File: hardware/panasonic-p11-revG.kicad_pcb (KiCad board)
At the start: 2 copper layers, 48.5 x 18 mm, 10 parts, among them J1 1x4, J11 1.27_RA_8way, J2 1x4

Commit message: hardware: J1/J2 expansion headers to 2.54mm pitch
Standard 0.1in header spacing with 1.7mm pads, repositioned to clear the
tie holes and board edge; re-routed and re-verified (all 14 nets correct,
CNT pin 4 isolated, 0 DRC, silk clean). Gerber zip regenerated.

Co-Authored-By: Claude Opus 5 <noreply@anthropic.com>
Claude-Session: https://claude.ai/code/session_01BQkgfhAH12YMdeYMtUUmA3
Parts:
- J1: footprint local:J2 -> local:J1
- J2: footprint local:J3 -> local:J2
- moved J1 1.63 mm to (60.0, 24.3)
- moved J2 1.63 mm to (60.0, 39.7)
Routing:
- net AC_RX_5V: track 16.9 -> 27.4 mm, vias 0 -> 1
- net GND: track 65.3 -> 60.8 mm
- net IO10_5V: track 19.9 -> 16.9 mm
- net +3V3: track 40.6 -> 43.4 mm, vias 0 -> 1
- net IO0: track 22.0 -> 19.6 mm
- net IO7_5V: track 10.2 -> 7.79 mm
- net AC_5V: track 24.3 -> 25.7 mm
- net +5V: track 66.1 -> 64.9 mm
- net IO1: track 25.3 -> 25.5 mm, vias 2 -> 3

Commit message: hardware: keep back-silk annotations clear of the through-hole pads
The URL and two other back-silk lines crossed the ESP32 pad row and would
be clipped by the mask openings. Whole block compacted into the clear
window between the pad rows; silkscreen checker extended to test back-side
text against pads so this is caught in future.

Co-Authored-By: Claude Opus 5 <noreply@anthropic.com>
Claude-Session: https://claude.ai/code/session_01BQkgfhAH12YMdeYMtUUmA3
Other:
- board text added: "CNT: CN-CNT 5p PIN4=12V NO CONN"
- board text added: "D1: 1N5819 C1: 100uF/16V"
- board text added: "J2: IO10 IO7 GND 5V (in only)"
- board text added: "LLC: BSS138 2-ch module 10.16mm"
- board text removed: "CNT: CN-CNT 5-pin PIN4=12V NO CONNECT"
- board text removed: "D1: 1N5819 C1: 100uF/16V radial"
- board text removed: "J2: IO10 IO7 GND 5V (input only)"
- board text removed: "LLC: BSS138 2-ch module (10.16mm rows)"
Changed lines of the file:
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@@
 	)
 	(gr_text "github.com/bl0ckstat/esphome-panasonic-ac"
-		(at 33.5 40.1 0)
+		(at 31.2 38.15 0)
 		(layer "B.SilkS")
 		(effects
 			(font
-				(size 0.6 0.6)
-				(thickness 0.13)
+				(size 0.55 0.55)
+				(thickness 0.11)
 			)
 			(justify mirror)
@@
 	)
 	(gr_text "MCU: ESP32-C3 SuperMini"
-		(at 31.5 27.3 0)
+		(at 31.2 27.35 0)
 		(layer "B.SilkS")
 		(effects
 			(font
-				(size 0.65 0.65)
-				(thickness 0.13)
+				(size 0.6 0.6)
+				(thickness 0.11)
 			)
 			(justify mirror)
 		)
 	)
-	(gr_text "LLC: BSS138 2-ch module (10.16mm rows)"
-		(at 31.5 28.9 0)
+	(gr_text "LLC: BSS138 2-ch module 10.16mm"
+		(at 31.2 28.7 0)
 		(layer "B.SilkS")
 		(effects
 			(font
-				(size 0.65 0.65)
-				(thickness 0.13)
+				(size 0.6 0.6)
+				(thickness 0.11)
 			)
 			(justify mirror)
 		)
 	)
-	(gr_text "D1: 1N5819   C1: 100uF/16V radial"
-		(at 31.5 30.5 0)
+	(gr_text "D1: 1N5819  C1: 100uF/16V"
+		(at 31.2 30.05 0)
 		(layer "B.SilkS")
 		(effects
 			(font
-				(size 0.65 0.65)
-				(thickness 0.13)
+				(size 0.6 0.6)
+				(thickness 0.11)
 			)
 			(justify mirror)
@@
 	)
 	(gr_text "J11: CN-WLAN (DNSK-P11) 1.27mm"
-		(at 31.5 32.1 0)
+		(at 31.2 31.4 0)
 		(layer "B.SilkS")
 		(effects
 			(font
-				(size 0.65 0.65)
-				(thickness 0.13)
+				(size 0.6 0.6)
+				(thickness 0.11)
 			)
 			(justify mirror)
 		)
 	)
-	(gr_text "CNT: CN-CNT 5-pin  PIN4=12V NO CONNECT"
-		(at 31.5 33.7 0)
+	(gr_text "CNT: CN-CNT 5p PIN4=12V NO CONN"
+		(at 31.2 32.75 0)
 		(layer "B.SilkS")
 		(effects
 			(font
-				(size 0.65 0.65)
-				(thickness 0.13)
+				(size 0.6 0.6)
+				(thickness 0.11)
 			)
 			(justify mirror)
@@
 	)
 	(gr_text "J1: IO1 IO0 GND 3V3 (direct)"
-		(at 31.5 35.3 0)
+		(at 31.2 34.1 0)
 		(layer "B.SilkS")
 		(effects
 			(font
-				(size 0.65 0.65)
-				(thickness 0.13)
+				(size 0.6 0.6)
+				(thickness 0.11)
 			)
 			(justify mirror)
 		)
 	)
-	(gr_text "J2: IO10 IO7 GND 5V (input only)"
-		(at 31.5 36.9 0)
+	(gr_text "J2: IO10 IO7 GND 5V (in only)"
+		(at 31.2 35.45 0)
 		(layer "B.SilkS")
 		(effects
 			(font
-				(size 0.65 0.65)
-				(thickness 0.13)
+				(size 0.6 0.6)
+				(thickness 0.11)
 			)
 			(justify mirror)
 		)
 	)
-	(gr_text "UART 9600 8E1  TX=IO3 RX=IO4"
-		(at 31.5 38.5 0)
+	(gr_text "UART 9600 8E1 TX=IO3 RX=IO4"
+		(at 31.2 36.8 0)
 		(layer "B.SilkS")
 		(effects
 			(font
-				(size 0.65 0.65)
-				(thickness 0.13)
+				(size 0.6 0.6)
+				(thickness 0.11)
 			)
 			(justify mirror)
@@
 	)
 	(gr_text "PANASONIC AC INTERFACE  rev G"
-		(at 31.5 25.4 0)
+		(at 31.2 26 0)
 		(layer "B.SilkS")
 		(effects
 			(font
-				(size 0.8 0.8)
-				(thickness 0.13)
+				(size 0.65 0.65)
+				(thickness 0.11)
 			)
 			(justify mirror)

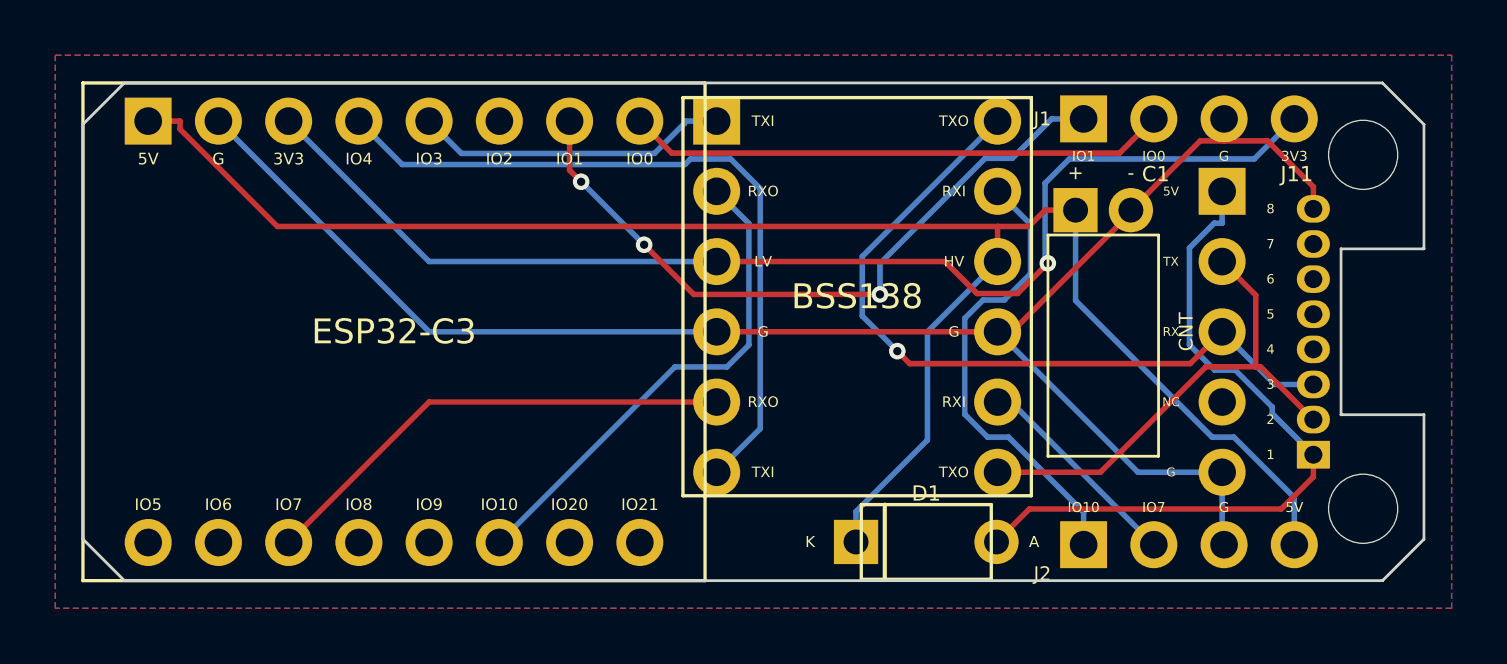
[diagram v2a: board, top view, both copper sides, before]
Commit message: hardware: fix ESP/LLC module body collision, add assembly view + parts list
The BSS138 module body overlapped the ESP32 SuperMini's end by 0.7mm - a
mechanical collision DRC could not see (no courtyards). Module moved 1mm
right (now 0.3mm gap), C1 nudged with it, board re-routed and re-verified
(all nets correct, 0 DRC, silk clean). Adds a to-scale populated-board
illustration and an AliExpress shopping list to the docs.

Co-Authored-By: Claude Opus 5 <noreply@anthropic.com>
Claude-Session: https://claude.ai/code/session_01BQkgfhAH12YMdeYMtUUmA3
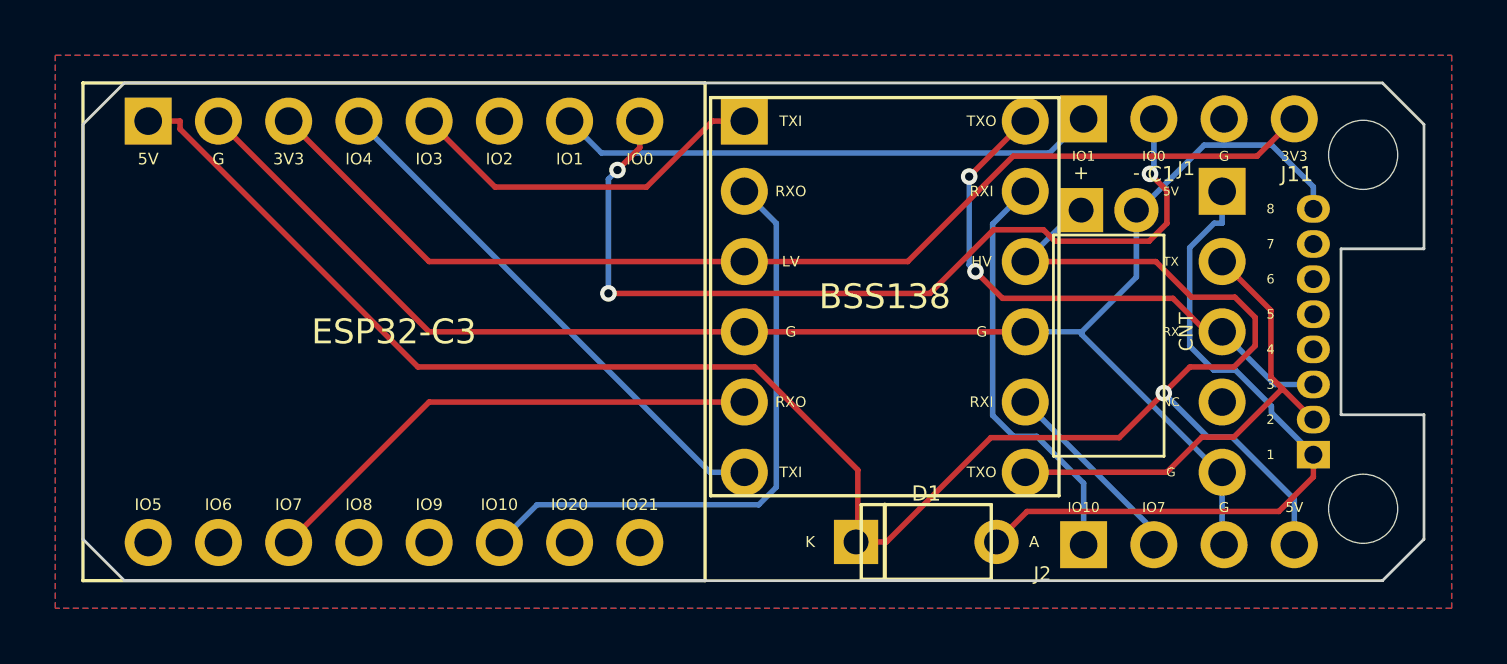
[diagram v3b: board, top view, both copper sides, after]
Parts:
- moved BSS138 1.00 mm to (49.0, 30.7)
- moved C1 0.20 mm to (57.1, 27.6)
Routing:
- net IO0: track 19.6 -> 32.4 mm, vias 0 -> 3
- net ESP_RX: track 26.6 -> 19.2 mm
- net AC_RX_5V: track 27.4 -> 20.3 mm, vias 1 -> 2
- net +5V: track 64.9 -> 72.0 mm, vias 0 -> 1
- net IO1: track 25.5 -> 19.6 mm, vias 3 -> 0
- net IO10: track 18.0 -> 22.0 mm
- net +3V3: track 43.4 -> 40.6 mm, vias 1 -> 0
- net ESP_TX: track 11.4 -> 13.4 mm
- net IO10_5V: track 16.9 -> 15.1 mm
- net GND: track 60.8 -> 59.2 mm
- net IO7: track 17.6 -> 18.6 mm
- net IO7_5V: track 7.79 -> 7.09 mm
